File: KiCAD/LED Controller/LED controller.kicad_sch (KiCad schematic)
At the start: 41 parts, among them J1 Barrel_Jack_Switch, J2 4x RJ45, J3 Conn_01x24_Female, J4 Conn_01x24_Female, J5 8P8C_Shielded, SW1 ELUMOASAQ2C22, SW2 ELUMOASAQ2C22, SW3 ELUMOASAQ2C22, U1 SN75374D, U2 SN75374D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

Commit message: Labels added
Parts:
- added SYM1: Logo_Open_Hardware_Small, Custom Footprints:CC-BY-SA Symbol, symbol Graphic:Logo_Open_Hardware_Small
- added SYM2: Logo_Open_Hardware_Small, Symbol:OSHW-Logo_5.7x6mm_SilkScreen, symbol Graphic:Logo_Open_Hardware_Small
- added SYM3: Logo_Center_Positive, Custom Footprints:Polarity, symbol Graphic:Logo_Open_Hardware_Small

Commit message: I2C and external LED connector added - Pass DRC
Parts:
- added C12: 220µF, Capacitor_THT:CP_Radial_D6.3mm_P2.50mm, symbol Device:C_Polarized_Small_US
- added J6: Conn_01x03_Socket, Connector_PinSocket_2.54mm:PinSocket_1x03_P2.54mm_Vertical_SMD_Pin1Left, symbol Connector:Conn_01x03_Socket
- added J7: Conn_01x02_Socket, Connector_PinSocket_2.54mm:PinSocket_1x02_P2.54mm_Vertical, symbol Connector:Conn_01x02_Socket
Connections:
- net 12V: now also C12.1
- net Ctrl1: now also J6.2 (Pin_2)
- net Ctrl2: now also J6.3 (Pin_3)
- net Ctrl3: now also J6.1 (Pin_1)
- net GND: now also C12.2
- net SCL: now also J7.1 (Pin_1)
- net SDA: now also J7.2 (Pin_2)

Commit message: Minor changes - ground strip along RJ45 12V, add part # for I2C socket
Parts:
- J7: Manufacturer (none) -> Adam Tech; Part (none) -> RS1-02-G
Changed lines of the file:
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@@
 			)
 		)
-		(property "Datasheet" "~"
+		(property "Datasheet" "https://app.adam-tech.com/products/download/data_sheet/203013/rs1-xx-g-data-sheet.pdf"
 			(at 161.29 133.35 0)
 			(effects
@@
 			)
 		)
-		(property "Description" "Generic connector, single row, 01x02, script generated"
+		(property "Description" "RECEPTACLE STRIP 2P 2.54MM PITCH"
 			(at 161.29 133.35 0)
 			(effects
@@
 			)
 		)
-		(property "Manufacturer" ""
+		(property "Manufacturer" "Adam Tech"
 			(at 161.29 133.35 0)
 			(effects
@@
 			)
 		)
-		(property "Part" ""
+		(property "Part" "RS1-02-G"
 			(at 161.29 133.35 0)
 			(effects

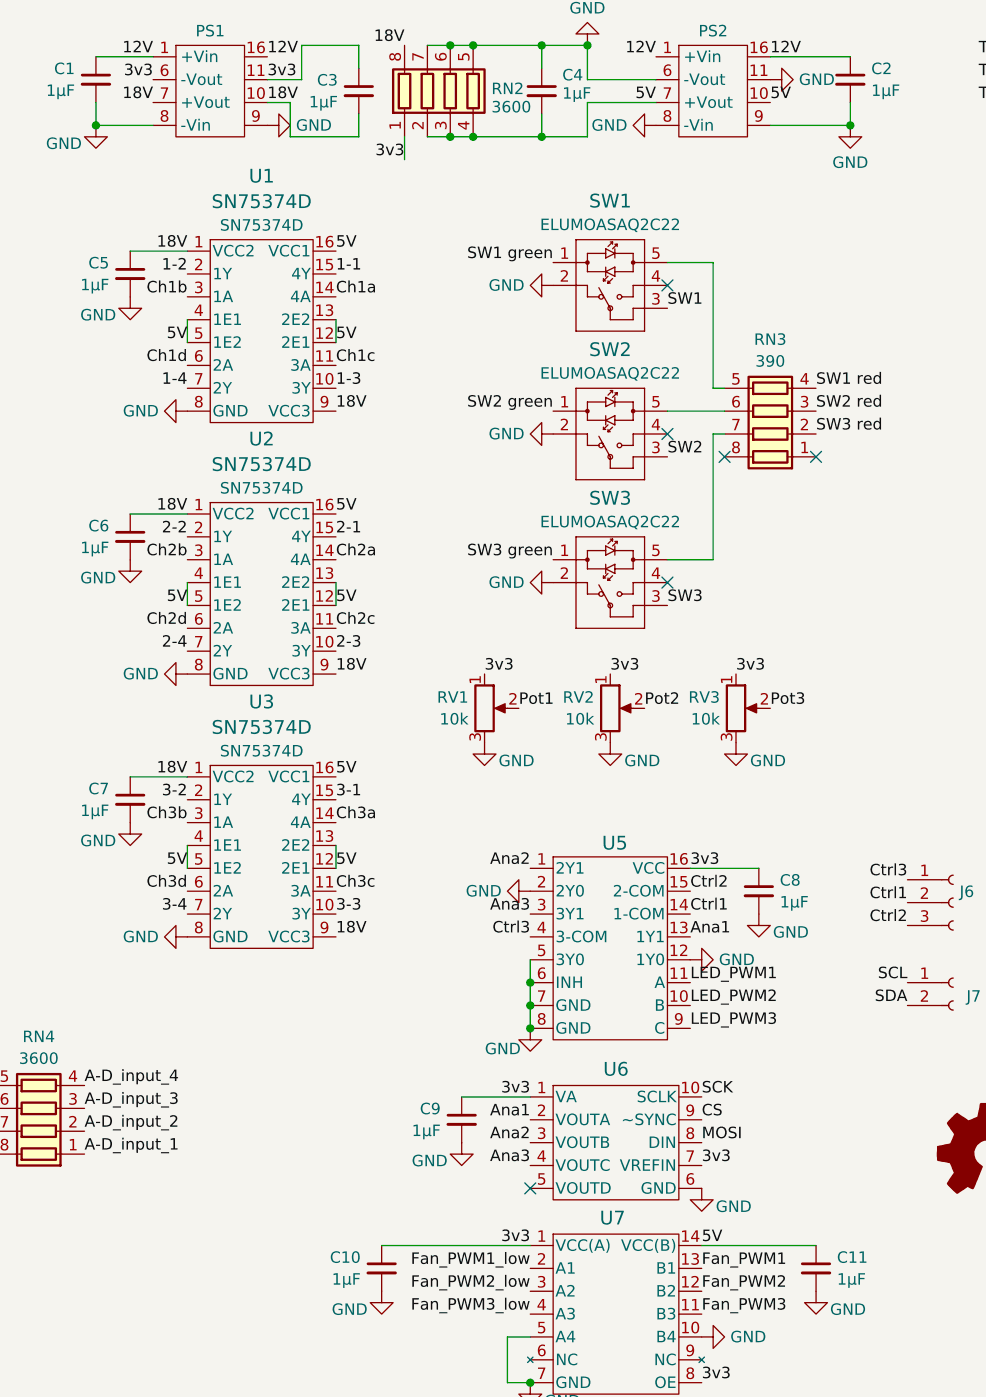
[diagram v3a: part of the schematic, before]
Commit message: Label schematic - switch to 10-bit DAC
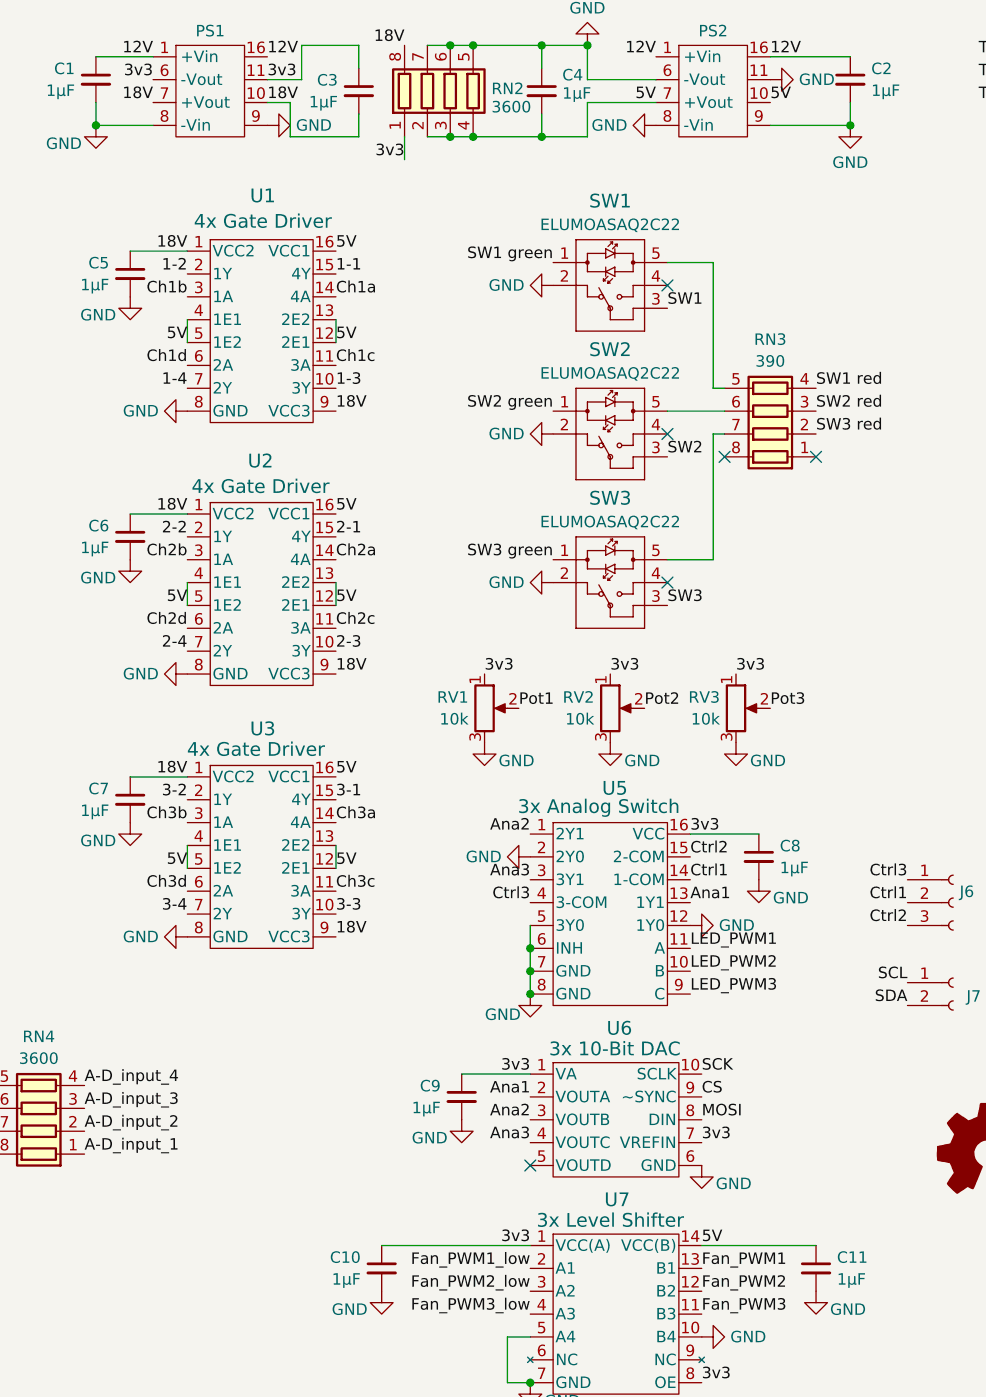
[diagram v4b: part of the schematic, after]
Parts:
- RV1, RV2, RV3: Part P160KN2-4QC20B10K -> P160KN2-0QA25B10K
- U1, U2, U3: value SN75374D -> 4x Gate Driver
- U5: value SN74LV4053ADR -> 3x Analog Switch
- U6: value DAC084S085CIMMX/NOPB -> 3x 10-Bit DAC; Part DAC084S085CIMMX/NOPB -> DAC104S085QIMMX/NOPB
- U7: value NXB0104PWJ -> 3x Level Shifter
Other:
- moved on the sheet: C8, C9, U5, U6
